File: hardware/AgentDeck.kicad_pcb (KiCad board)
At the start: 4 copper layers, 95 x 95 mm, 101 parts, among them J1 USB-C, J2 SWD, SW1 K1, SW10 K10, SW11 K11, SW12 K12, SW13 BOOTSEL, SW14 CONN-SMD_HOTPLUGPAKAGE__C9900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, SW2 K2, SW3 K3, SW4 K4, SW5 K5, SW6 K6, SW7 K7, SW8 K8, SW9 K9, U1 RP2040, U2 W25Q128JVSIQ, U3 AMS1117-3.3, U4 74AHCT1G125, U6 USBLC6-2SC6, Y1 ABM8-272-T3

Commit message: route cage nets
Freerouting 2.3.0 with the pocket cage (K1/K5/K6/K8/K9/K10) ripped and GND
pinned through U1-19/57 + C12 solved the two 'impossible' connections:
pad 10 (+3V3) is now routed and the GND cluster join was built by the router.
Subsequent iterations landed K5/K8/K9/K10 but rip up the GND join when
re-routing (imported wiring is not fixed), oscillating at 3 unconnected.
Current best adopted state: 0 DRC errors, 3 unconnected (U1-19 GND join,
K1 SW1->U1, K6 SW6->U1). These three want interactive routing.
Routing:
- net K1: track 76.9 -> 0.00 mm, vias 2 -> 0
- net K6: track 67.0 -> 0.00 mm, vias 3 -> 0
- net K5: track 52.6 -> 83.6 mm, vias 3 -> 4
- net K10: track 48.4 -> 64.9 mm, vias 3 -> 4
- net K9: track 42.0 -> 30.9 mm
- net +3V3: track 182.3 -> 190.7 mm, vias 11 -> 12
- net K8: track 45.7 -> 43.3 mm, vias 3 -> 2

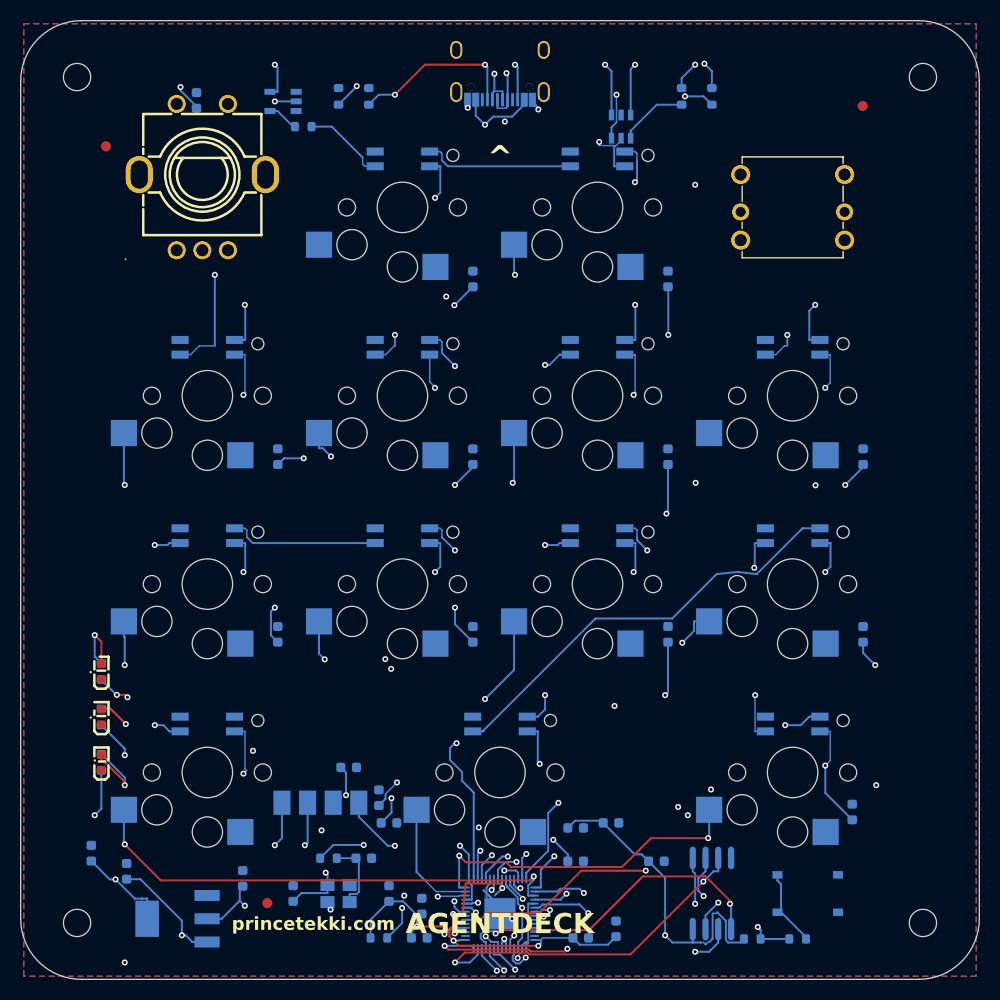
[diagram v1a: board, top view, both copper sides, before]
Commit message: restore best routed state
The cage-net campaign (K1 via donor transplant etc.) net-regressed from 2 to
5 unconnected - each win evicted an equal loss; the pocket is at capacity in
that era's layout. e5d29c3's board is the best known: 0 errors, 2 unconnected
(pin-19 GND join, pad-10 +3V3). Kept cage-era wiring as a donor in scratch.
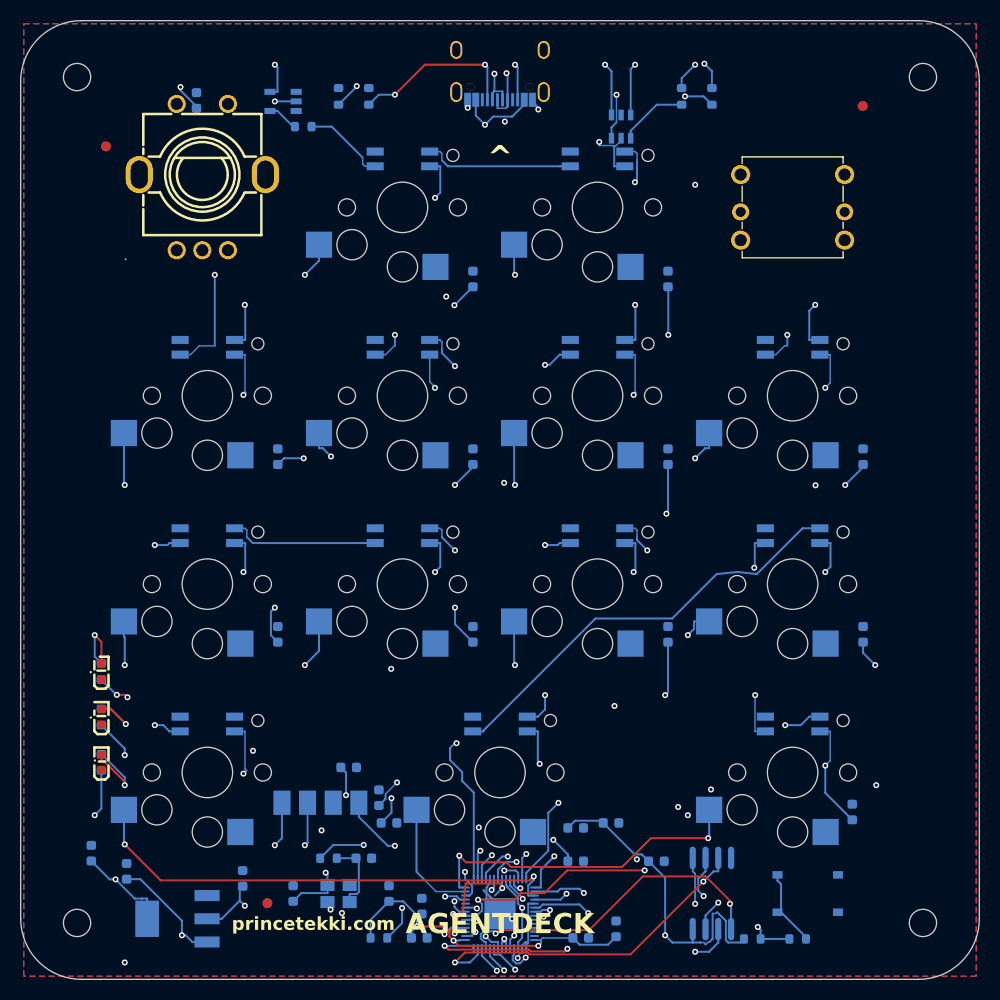
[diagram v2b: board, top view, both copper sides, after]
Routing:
- net K1: track 0.00 -> 76.9 mm, vias 0 -> 2
- net K6: track 0.00 -> 67.0 mm, vias 0 -> 3
- net K5: track 83.6 -> 52.6 mm, vias 4 -> 3
- net K10: track 64.9 -> 48.4 mm, vias 4 -> 3
- net K9: track 30.9 -> 42.0 mm
- net +3V3: track 190.7 -> 182.3 mm, vias 12 -> 11
- net K8: track 43.3 -> 45.7 mm, vias 2 -> 3
